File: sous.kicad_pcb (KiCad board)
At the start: 2 copper layers, 99.8 x 38.1 mm, 45 parts, among them CON1 USB Power, IC1 ATMEGA328P-P, P1 ISP, P2 FTDI/serial/BT, SW1 RESET, U1 COM-10982, U2 74HC595, U3 DS18B20, U4 74LS14, U5 ULN2003

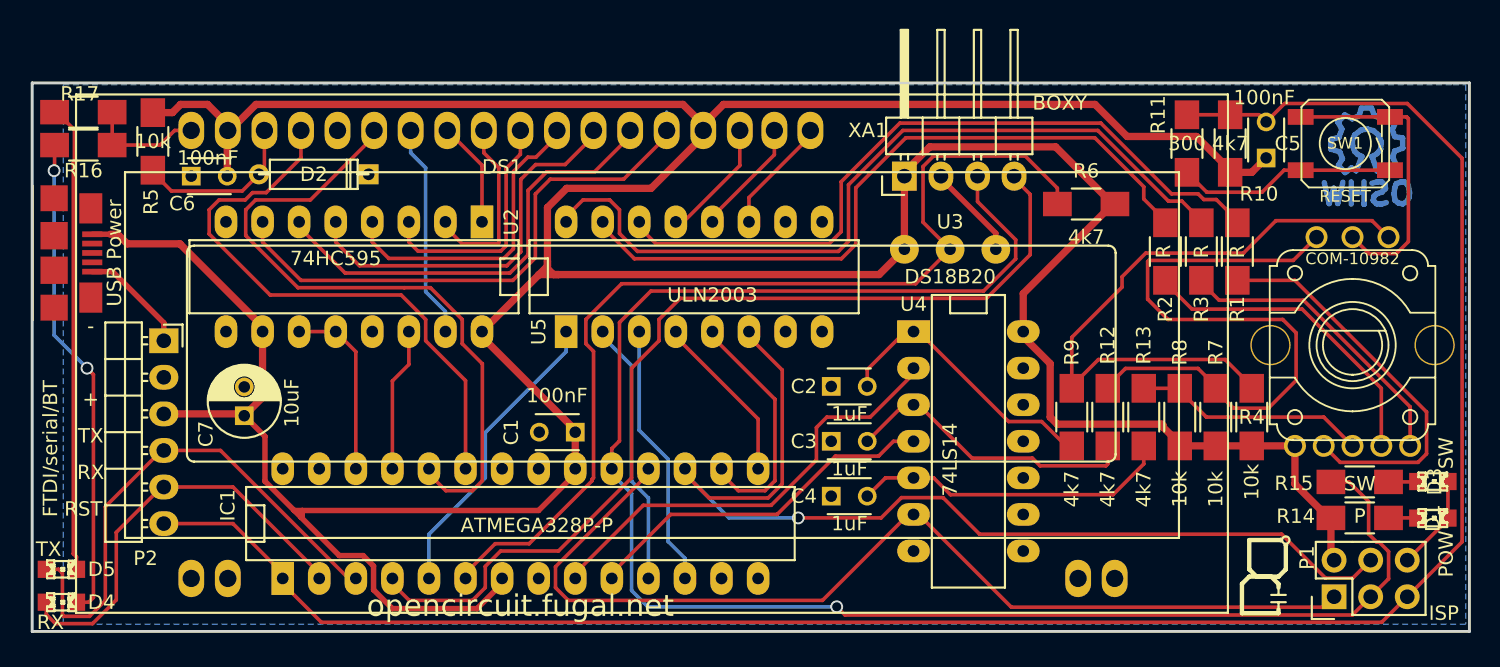
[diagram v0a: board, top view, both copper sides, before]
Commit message: Updated to newer kicad, fixed tx/rx swap
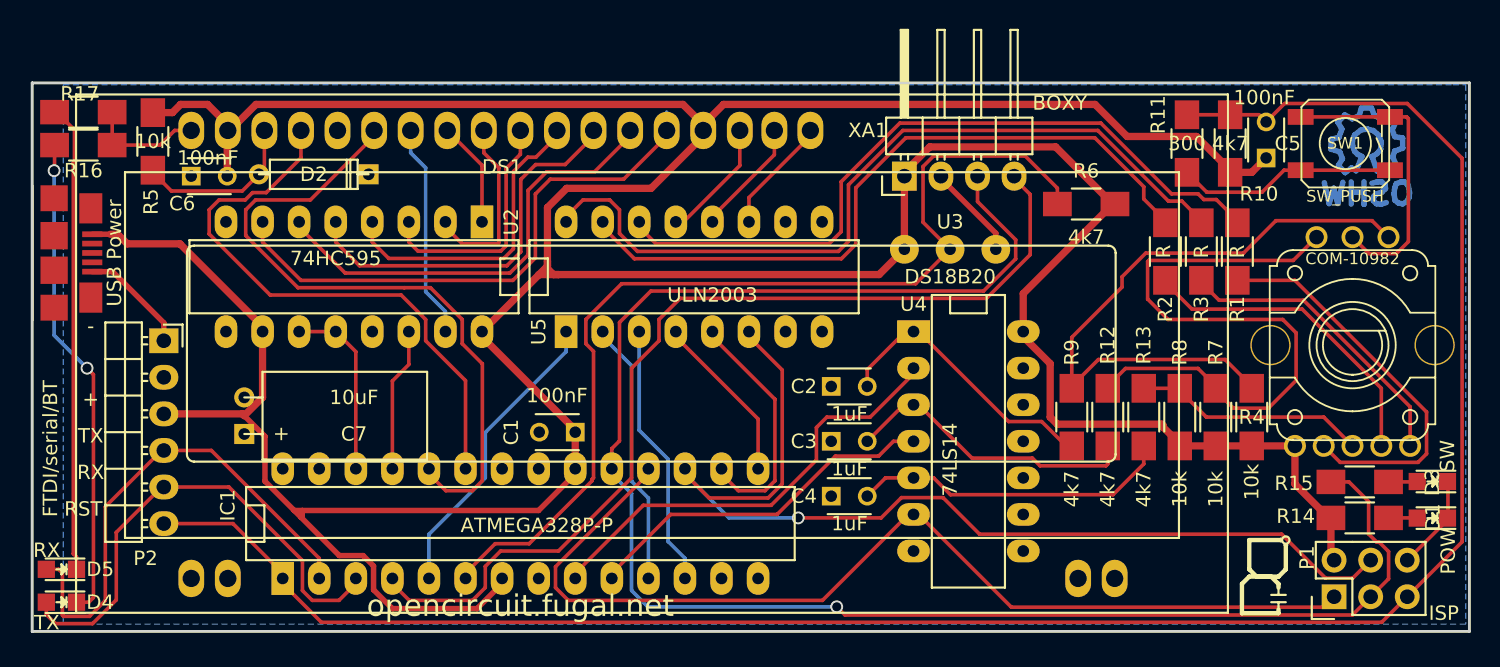
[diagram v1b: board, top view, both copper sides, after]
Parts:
- C7: footprint Capacitors_ThroughHole:C_Radial_D5_L11_P2 -> Discret:C1V5H
- D1, D3: footprint LEDs:LED-0805 -> LEDs:LED_0805
- D4: value RX -> TX; footprint LEDs:LED-0805 -> LEDs:LED_0805
- D5: value TX -> RX; footprint LEDs:LED-0805 -> LEDs:LED_0805
- R14: value P -> Power
- R15: value SW -> Switch
- SW1: value RESET -> SW_PUSH
- turned D1 to 180 degrees
- turned D3 to 180 degrees
- turned D4 to 180 degrees
- turned D5 to 180 degrees
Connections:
- net /Debounce/Out3 renamed /MISO
- net VCC renamed +5V
- D1 pad 1: Net-(D1-Pad1) -> GND
- D1 pad 2: GND -> Net-(D1-Pad2)
- D2 pad 1: Net-(D2-Pad1) -> GND
- D2 pad 2: GND -> Net-(D2-Pad2)
- D3 pad 1: Net-(D3-Pad1) -> GND
- D3 pad 2: GND -> Net-(D3-Pad2)
- D4 pad 1: /RX -> Net-(D4-Pad1)
- D4 pad 2: Net-(D4-Pad2) -> /TX
- D5 pad 1: /TX -> Net-(D5-Pad1)
- D5 pad 2: Net-(D5-Pad2) -> /RX
- DS1 pad 3: Net-(D2-Pad1) -> Net-(D2-Pad2)
- P2 pad 4: /TX -> /RX
- P2 pad 5: /RX -> /TX
- R14 pad 2: Net-(D1-Pad1) -> Net-(D1-Pad2)
- R15 pad 2: Net-(D3-Pad1) -> Net-(D3-Pad2)
- R16 pad 2: Net-(D4-Pad2) -> Net-(D4-Pad1)
- R17 pad 2: Net-(D5-Pad2) -> Net-(D5-Pad1)
- R5 pad 1: Net-(D2-Pad1) -> Net-(D2-Pad2)
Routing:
- net Net-(D4-Pad2): track 33.9 -> 0.00 mm, vias 2 -> 0
- net Net-(D4-Pad1): track 0.00 -> 33.9 mm, vias 0 -> 2
- net Net-(D5-Pad2): track 32.5 -> 0.00 mm
- net Net-(D5-Pad1): track 0.00 -> 32.5 mm
- net Net-(D2-Pad2): track 0.00 -> 11.7 mm
- net Net-(D2-Pad1): track 11.7 -> 0.00 mm
- net /RX: track 29.6 -> 35.5 mm
- net /TX: track 36.8 -> 34.6 mm
- net Net-(D3-Pad2): track 0.00 -> 2.04 mm
- net Net-(D3-Pad1): track 2.04 -> 0.00 mm
- net Net-(D1-Pad2): track 0.00 -> 2.03 mm
- net Net-(D1-Pad1): track 2.03 -> 0.00 mm
